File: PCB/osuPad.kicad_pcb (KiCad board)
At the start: 2 copper layers, 66.7 x 47.6 mm, 8 parts, among them J1 OLED_128x32, U1 MCU_Seeed_XIAO_RP2040

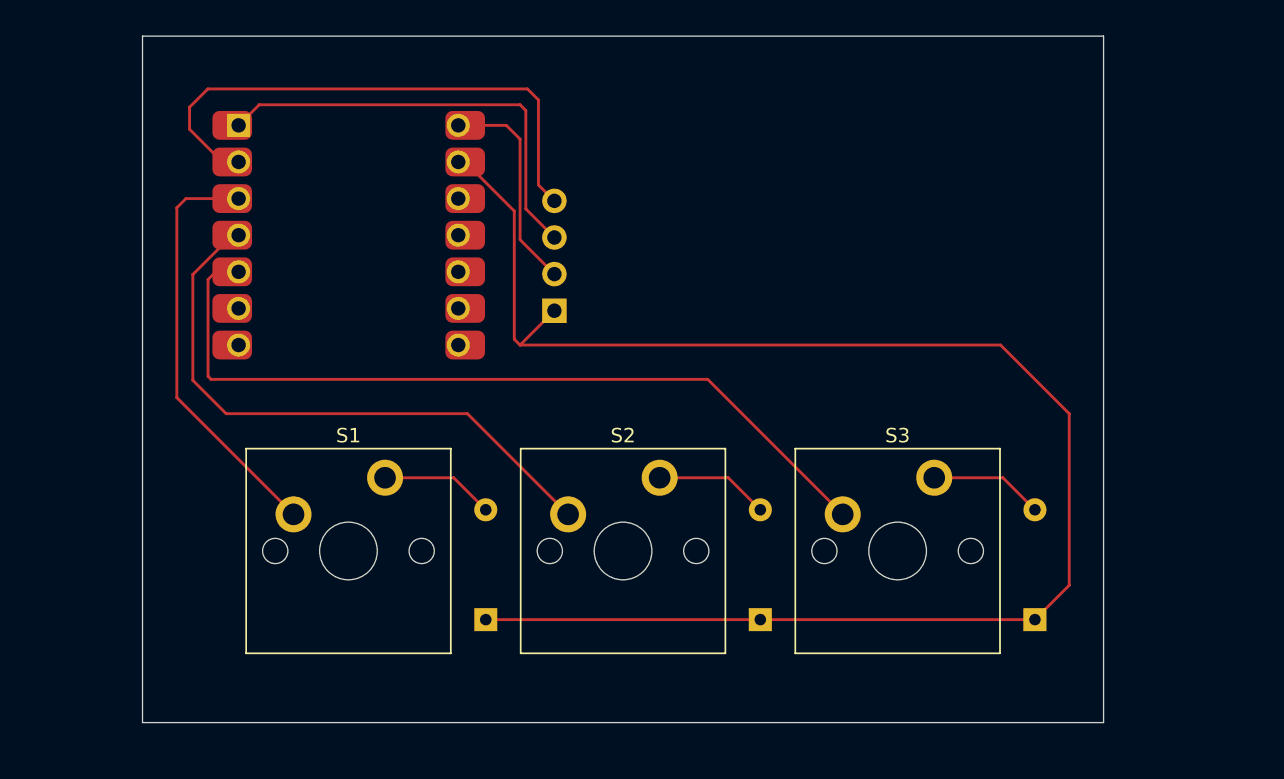
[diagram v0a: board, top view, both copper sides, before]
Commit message: add BOM
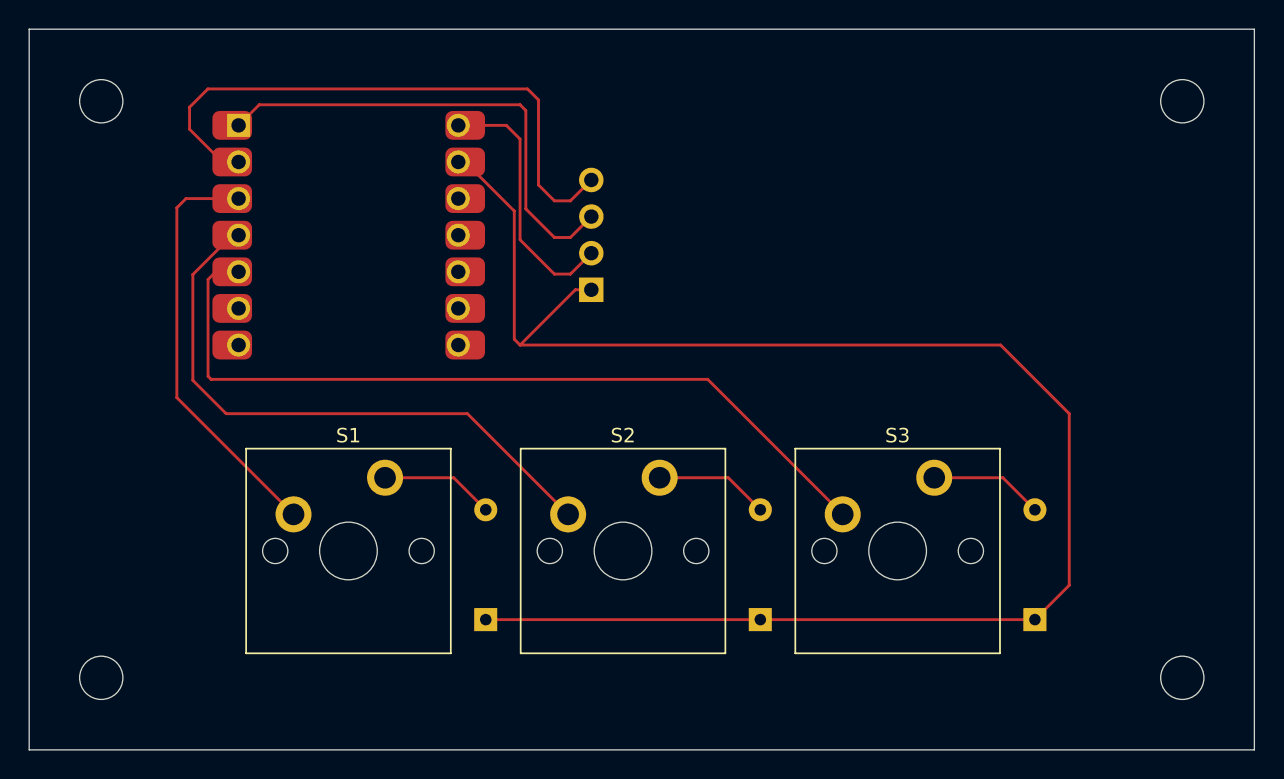
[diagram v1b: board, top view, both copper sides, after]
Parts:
- moved J1 2.94 mm to (72.4, 48.3)
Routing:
- net Net-(J1-SCL): track 30.3 -> 33.5 mm
- net Net-(J1-VCC): track 15.0 -> 18.2 mm
- net Net-(J1-SDA): track 39.0 -> 42.2 mm
- net Net-(D1-K): track 111.1 -> 114.3 mm
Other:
- board size 66.7 x 47.6 mm -> 85 x 50 mm
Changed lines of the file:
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@@
 	(footprint "ScottoKeebs_Components:OLED_128x32"
 		(layer "F.Cu")
-		(at 69.8375 49.73125)
+		(at 72.4 48.28)
 		(property "Reference" "J1"
 			(at 7.75 10 0)
@@
 		)
 		(embedded_fonts no)
-		(model "${SCOTTOKEEBS_KICAD}/3dmodels/ScottoKeebs_Components.3dshapes/OLED_128x32.step"
+		(model "${COTTKEBBS}/ScottoKeebs_Components.3dshapes/OLED_128x32.step"
 			(offset
 				(xyz 19 -6 2.5)
@@
 		)
 		(embedded_fonts no)
-		(model "${SCOTTOKEEBS_KICAD}/3dmodels/ScottoKeebs_MX.3dshapes/MX_PCB.step"
+		(model "${COTTKEBBS}/ScottoKeebs_MX.3dshapes/MX_PCB.step"
 			(offset
 				(xyz 0 0 0)
@@
 		)
 		(embedded_fonts no)
-		(model "${SCOTTOKEEBS_KICAD}/3dmodels/ScottoKeebs_MX.3dshapes/MX_PCB.step"
+		(model "${COTTKEBBS}/ScottoKeebs_MX.3dshapes/MX_PCB.step"
 			(offset
 				(xyz 0 0 0)
@@
 		)
 		(embedded_fonts no)
-		(model "${SCOTTOKEEBS_KICAD}/3dmodels/ScottoKeebs_MX.3dshapes/MX_PCB.step"
+		(model "${COTTKEBBS}/ScottoKeebs_MX.3dshapes/MX_PCB.step"
 			(offset
 				(xyz 0 0 0)
@@
 		)
 		(embedded_fonts no)
-		(model "${SCOTTOKEEBS_KICAD}/3dmodels/ScottoKeebs_MCU.3dshapes/Seeed_XIAO_RP2040.step"
+		(model "${COTTKEBBS}/ScottoKeebs_MCU.3dshapes/Seeed_XIAO_RP2040.step"
 			(offset
 				(xyz 0 0 0)
@@
 		)
 		(embedded_fonts no)
-		(model "${SCOTTOKEEBS_KICAD}/3dmodels/ScottoKeebs_Components.3dshapes/Diode_DO-35.step"
+		(model "${COTTKEBBS}/ScottoKeebs_Components.3dshapes/Diode_DO-35.step"
 			(offset
 				(xyz 0 0 0)
@@
 		)
 		(embedded_fonts no)
-		(model "${SCOTTOKEEBS_KICAD}/3dmodels/ScottoKeebs_Components.3dshapes/Diode_DO-35.step"
+		(model "${COTTKEBBS}/ScottoKeebs_Components.3dshapes/Diode_DO-35.step"
 			(offset
 				(xyz 0 0 0)
@@
 		)
 		(embedded_fonts no)
-		(model "${SCOTTOKEEBS_KICAD}/3dmodels/ScottoKeebs_Components.3dshapes/Diode_DO-35.step"
+		(model "${COTTKEBBS}/ScottoKeebs_Components.3dshapes/Diode_DO-35.step"
 			(offset
 				(xyz 0 0 0)
@@
 		)
 	)
-	(gr_rect
-		(start 42.8625 40.48125)
-		(end 109.5375 88.10625)
+	(gr_circle
+		(center 40 45)
+		(end 40 46.5)
 		(stroke
 			(width 0.05)
@@
 		(layer "Edge.Cuts")
 	)
+	(gr_circle
+		(center 115 45)
+		(end 115 46.5)
+		(stroke
+			(width 0.05)
+			(type default)
+		)
+		(fill no)
+		(layer "Edge.Cuts")
+	)
+	(gr_rect
+		(start 35 40)
+		(end 120 90)
+		(stroke
+			(width 0.05)
+			(type default)
+		)
+		(fill no)
+		(layer "Edge.Cuts")
+	)
+	(gr_circle
+		(center 40 85)
+		(end 40 86.5)
+		(stroke
+			(width 0.05)
+			(type default)
+		)
+		(fill no)
+		(layer "Edge.Cuts")
+	)
+	(gr_circle
+		(center 115 85)
+		(end 115 86.5)
+		(stroke
+			(width 0.05)
+			(type default)
+		)
+		(fill no)
+		(layer "Edge.Cuts")
+	)
 	(segment
 		(start 107.15625 66.675)
@@
 	)
 	(segment
-		(start 71.4375 59.53125)
-		(end 69.05625 61.9125)
+		(start 72.88875 58.08)
+		(end 74 58.08)
 		(width 0.2)
 		(layer "F.Cu")
@@
 	)
 	(segment
+		(start 69.05625 61.9125)
+		(end 72.88875 58.08)
+		(width 0.2)
+		(layer "F.Cu")
+		(net 1)
+	)
+	(segment
 		(start 68.65525 52.61775)
 		(end 65.25 49.2125)
@@
 	(segment
 		(start 71.4375 56.99125)
+		(end 72.54875 56.99125)
+		(width 0.2)
+		(layer "F.Cu")
+		(net 10)
+	)
+	(segment
+		(start 71.4375 56.99125)
 		(end 69.05625 54.61)
 		(width 0.2)
@@
 	)
 	(segment
+		(start 72.54875 56.99125)
+		(end 74 55.54)
+		(width 0.2)
+		(layer "F.Cu")
+		(net 10)
+	)
+	(segment
 		(start 69.45725 52.471)
 		(end 69.45725 45.64475)
@@
 	)
 	(segment
+		(start 72.54875 54.45125)
+		(end 74 53)
+		(width 0.2)
+		(layer "F.Cu")
+		(net 11)
+	)
+	(segment
+		(start 71.4375 54.45125)
+		(end 72.54875 54.45125)
+		(width 0.2)
+		(layer "F.Cu")
+		(net 11)
+	)
+	(segment
 		(start 69.05625 45.24375)
 		(end 50.95875 45.24375)
@@
 	)
 	(segment
+		(start 71.4375 51.91125)
+		(end 72.54875 51.91125)
+		(width 0.2)
+		(layer "F.Cu")
+		(net 12)
+	)
+	(segment
 		(start 46.1264 45.4152)
 		(end 46.1264 46.94027)
@@
 		(width 0.2)
 		(layer "F.Cu")
+		(net 12)
+	)
+	(segment
+		(start 72.54875 51.91125)
+		(end 74 50.46)
+		(width 0.2)
+		(layer "F.Cu")
